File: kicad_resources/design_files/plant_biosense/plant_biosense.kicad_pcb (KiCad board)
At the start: 2 copper layers, 187 x 124.5 mm, 73 parts, among them J1 RJ45_Shielded, J2 RJ45_Shielded, U1 LM7805_TO220, U10 OP07, U11 TXS0108EPW, U12 OP07, U13 TL081, U14 NodeMCU1.0(ESP-12E), U15 ADS1115IDGS, U2 CD4051B, U3 CD4051B, U4 2S4P LI-ION BATTERY, U5 2S LI-ION BMS 10A, U7 XL4015, U8 AD620_instrumentation_amplifi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, U9 INA219AxD

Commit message: Initial public release: add CHL, docs, schematics
Adds CEREPHYTE Hardware License (CHL v1.0), NOTICE, CHANGELOG and THIRD_PARTY attribution; updates README. Adds multiple schematic PDFs under SCHEMATICS. Updates KiCad plant_biosense files (rev 4.2): date/revision bump, net/pad fixes (Net-(A1-D13)), pin type change, netclass/property and several wiring/no_connect adjustments. Prepares repository for public release and clarifies third-party licensing for included kicad-ESP8266 files.
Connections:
- A1 pad 28: unconnected-(A1-D13-Pad28) -> Net-(A1-D13)
- J2 pad 3: Net-(A1-D11) -> Net-(A1-D13)
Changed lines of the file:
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@@
 			(layers "*.Cu" "*.Mask")
 			(remove_unused_layers no)
-			(net "Net-(A1-D11)")
+			(net "Net-(A1-D13)")
 			(pintype "passive")
 		)
@@
 			(layers "*.Cu" "*.Mask")
 			(remove_unused_layers no)
-			(net "unconnected-(A1-D13-Pad28)")
+			(net "Net-(A1-D13)")
 			(pinfunction "D13_28")
-			(pintype "bidirectional+no_connect")
+			(pintype "bidirectional")
 		)
 		(pad "29" thru_hole oval

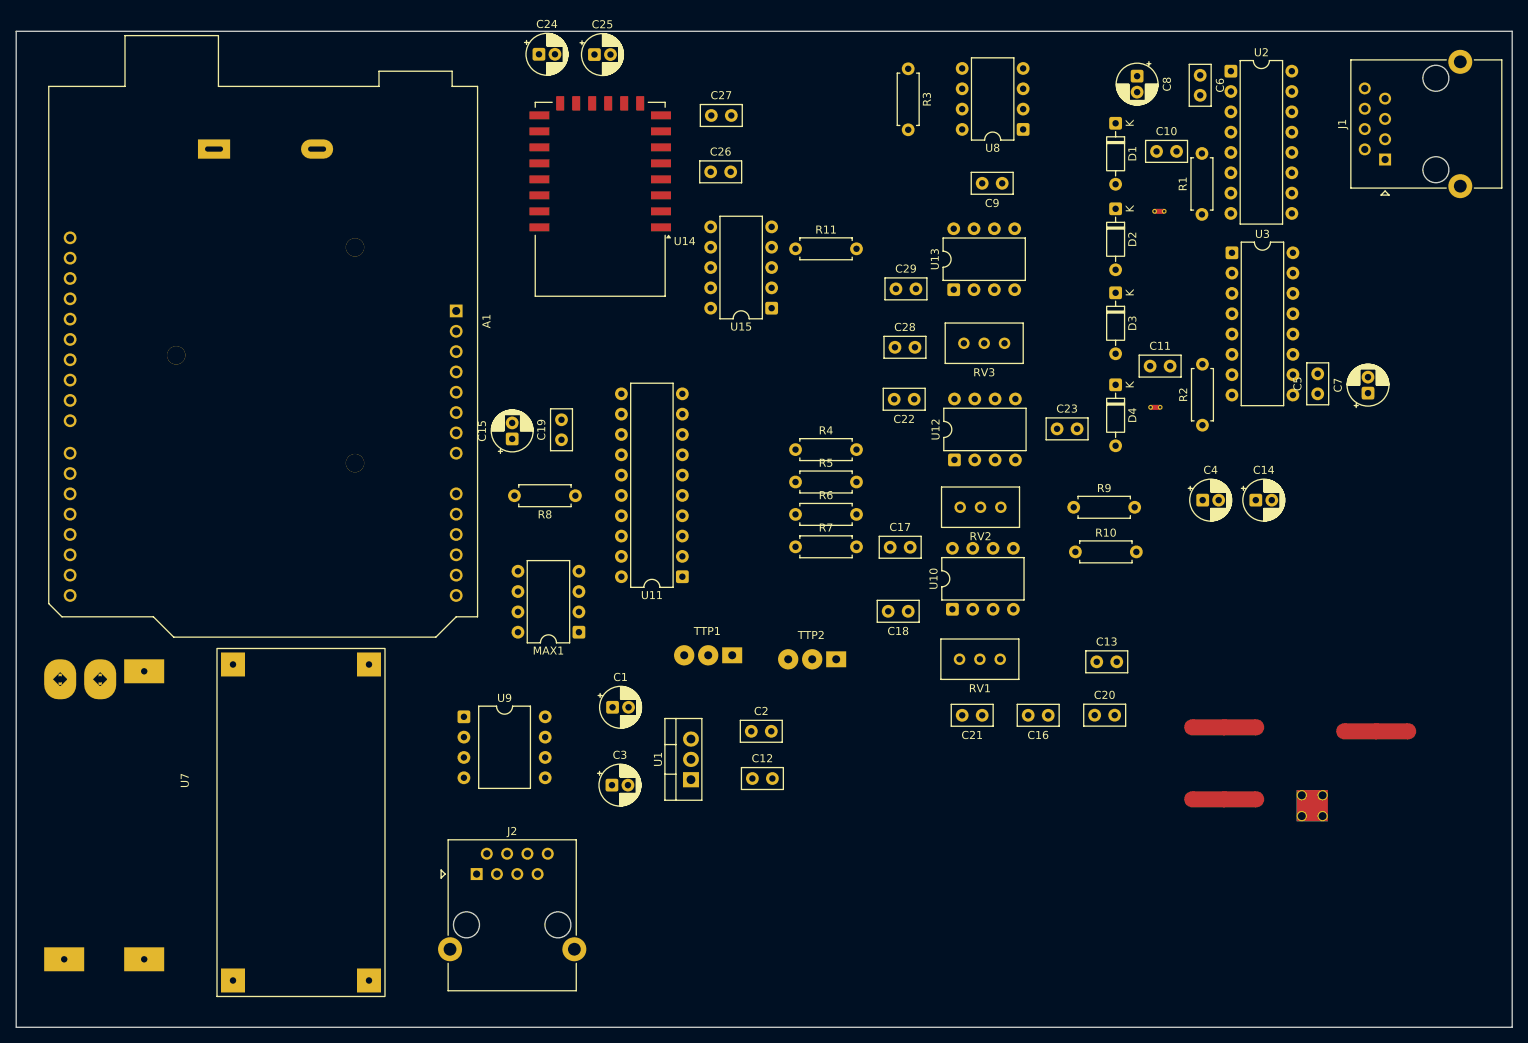
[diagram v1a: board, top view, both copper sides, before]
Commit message: 16 october 2026
Finalize CEREPHYTE Rev. 4.2 schematic architecture

- Finalize power supply, analog front-end, ADC, and microcontroller architecture
- Configure XL4015 buck converter for regulated 5V VDD
- Document INA219 and ADS1115 I2C addresses
- Define split analog/digital grounding topology
- Prepare schematic for physical protoboard implementation

Author: Omm Prakash Das
Date: 2026-10-16
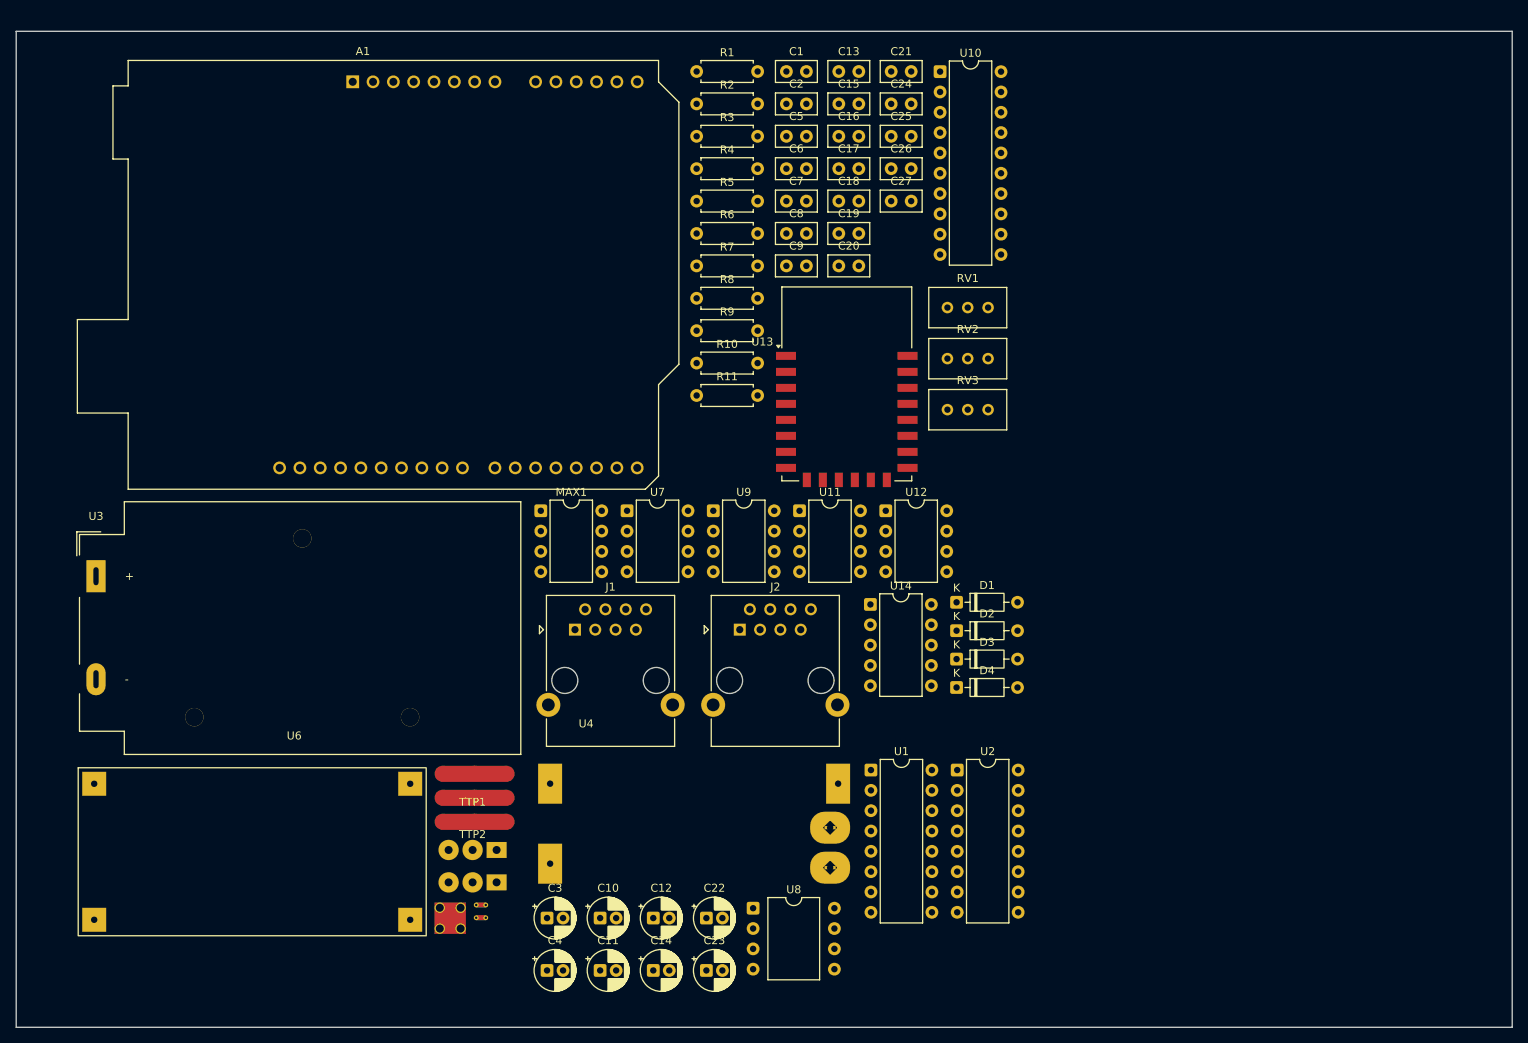
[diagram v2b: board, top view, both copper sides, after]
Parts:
- removed C28, C29: 0.1uf, Capacitor_THT:C_Disc_D5.0mm_W2.5mm_P2.50mm
- removed U15: ADS1115IDGS, Package_DIP:DIP-10_W7.62mm
- removed U5: 2S LI-ION BMS 10A, 2s LI-ION bms:2s LI-ION BMS 10A
- added U6: XL4015, XL4015 5A DC-DC Step Down Adjustable Power Supply Buck Module:XL4015 5A DC-DC Step Down Adjustable Power Supply Buck Mo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, F.Cu at (27.8, 111.6)
- C1, C15, C24, C25, C7, C8: value 10uf -> 0.1uf; footprint Capacitor_THT:CP_Radial_D5.0mm_P2.00mm -> Capacitor_THT:C_Disc_D5.0mm_W2.5mm_P2.50mm
- C10, C12, C22, C23: value 0.1uf -> 10uf; footprint Capacitor_THT:C_Disc_D5.0mm_W2.5mm_P2.50mm -> Capacitor_THT:CP_Radial_D5.0mm_P2.00mm
- C11: value 0.1uf -> 100uf; footprint Capacitor_THT:C_Disc_D5.0mm_W2.5mm_P2.50mm -> Capacitor_THT:CP_Radial_D5.0mm_P2.00mm
- C14: value 100uf -> 0.47uf
- C16, C20, C21: value 1uf -> 0.1uf
- C18, C19, C9: value 0.1uf -> 1uf
- C4: value 0.47uf -> 10uf
- U1: value LM7805_TO220 -> CD4051B; footprint Package_TO_SOT_THT:TO-220-3_Vertical -> Package_DIP:DIP-16_W7.62mm
- U10: value OP07 -> TXS0108EPW; footprint Package_DIP:DIP-8_W7.62mm -> Package_DIP:DIP-20_W7.62mm
- U11: value TXS0108EPW -> OP07; footprint Package_DIP:DIP-20_W7.62mm -> Package_DIP:DIP-8_W7.62mm
- U12: value OP07 -> TL081
- U13: value TL081 -> NodeMCU1.0(ESP-12E); footprint Package_DIP:DIP-8_W7.62mm -> RF_Module:ESP-12E
- U14: value NodeMCU1.0(ESP-12E) -> ADS1115IDGS; footprint RF_Module:ESP-12E -> Package_DIP:DIP-10_W7.62mm
- U3: value CD4051B -> 2S4P LI-ION BATTERY; footprint Package_DIP:DIP-16_W7.62mm -> Battery:BatteryHolder_MPD_BA9VPC_1xPP3
- U4: value 2S4P LI-ION BATTERY -> 2S LI-ION BMS 10A; footprint Battery:BatteryHolder_MPD_BA9VPC_1xPP3 -> 2s LI-ION bms:2s LI-ION BMS 10A; moved to F.Cu
- U7: value XL4015 -> AD620_instrumentation_amplifier_module; footprint XL4015 5A DC-DC Step Down Adjustable Power Supply Buck Module:XL4015 5A DC-DC Step Down Adjustable Power Supply Buck Mo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 -> Package_DIP:DIP-8_W7.62mm
- U8: value AD620_instrumentation_amplifier_module -> INA219AxD; footprint Package_DIP:DIP-8_W7.62mm -> Package_DIP:DIP-8_W10.16mm
- U9: value INA219AxD -> OP07; footprint Package_DIP:DIP-8_W10.16mm -> Package_DIP:DIP-8_W7.62mm
- moved U3 147.6 mm to (30.0, 87.6)
- moved NT1 121.3 mm to (77.5, 128.7)
- moved C10 118.4 mm to (93.0, 130.3)
- moved J1 117.1 mm to (89.8, 94.3), turned to 0 degrees
- moved NT4 113.0 mm to (77.3, 115.3)
- moved NT6 108.7 mm to (73.0, 129.1)
- moved NT2 105.7 mm to (77.5, 130.3)
- moved U8 103.0 mm to (112.1, 129.1), turned to 0 degrees
- moved C11 102.1 mm to (93.0, 136.9)
- moved C4 100.9 mm to (86.4, 136.9)
- moved C14 95.5 mm to (99.6, 136.9)
- moved NT3 93.9 mm to (77.3, 112.3)
- moved U2 93.8 mm to (137.6, 111.8)
- moved NT5 93.7 mm to (77.3, 118.3)
- moved U4 86.2 mm to (84.7, 110.5), turned to 0 degrees
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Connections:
- A1 pad 8: /PS_OUT+ -> /vdd
- C1 pad 2: GND -> GNDA
- C10 pad 1: /EESPC_out1 -> /vdd
- C10 pad 2: GNDA -> GND
- C11 pad 1: /EESPC_out2 -> GND
- C11 pad 2: GNDA -> /vee
- C12 pad 1: /PS_OUT+ -> /vdd
- C12 pad 2: /PS_OUT- -> GNDD
- C13 pad 1: Net-(U8-Vout) -> Net-(C13-Pad1)
- C13 pad 2: Net-(C13-Pad2) -> Net-(U9-+)
- C14 pad 1: GND -> /vdd
- C14 pad 2: /vee -> GND
- C15 pad 1: /PS_OUT+ -> GNDA
- C15 pad 2: GNDD -> Net-(U9-V+)
- C16 pad 1: Net-(C13-Pad2) -> /vee
- C16 pad 2: Net-(U10-+) -> GNDA
- C17 pad 1: GNDA -> /vdd
- C17 pad 2: Net-(U10-V+) -> GNDD
- C18 pad 1: /vee -> GNDA
- C18 pad 2: GNDA -> Net-(C18-Pad2)
- C19 pad 1: /PS_OUT+ -> GNDA
- C19 pad 2: GNDD -> Net-(U11-+)
- C2 pad 2: GND -> GNDA
- C20 pad 1: GNDA -> Net-(U11-V+)
- C20 pad 2: Net-(C20-Pad2) -> GNDA
- C21 pad 1: GNDA -> /vee
- C21 pad 2: Net-(U12-+) -> GNDA
- C22 pad 1: Net-(U12-V+) -> /vdd
- C22 pad 2: GNDA -> GNDD
- C23 pad 1: /vee -> /arduino5v
- C23 pad 2: GNDA -> GNDD
- C24 pad 1: /PS_OUT+ -> /arduino5v
- C25 pad 1: /arduino5v -> /vdd
- C26 pad 1: /arduino5v -> Net-(U12-V+)
- C26 pad 2: GNDD -> GNDA
- C27 pad 1: /PS_OUT+ -> /vee
- C27 pad 2: GNDD -> GNDA
- C3 pad 1: /PS_OUT+ -> /vdd
- C3 pad 2: GND -> GNDA
- C4 pad 1: /PS_OUT+ -> /vdd
- C4 pad 2: GND -> GNDA
- C5 pad 1: /vdd -> Net-(U7-vin)
- C6 pad 1: /vdd -> /EESPC_out1
- C7 pad 1: /vdd -> /EESPC_out2
- C8 pad 2: GNDA -> Net-(U6-OUT-)
- C9 pad 1: Net-(U8-vin) -> Net-(U7-Vout)
- C9 pad 2: GNDA -> Net-(C13-Pad1)
- NT3 pad 2: /PS_OUT- -> Net-(U6-OUT-)
- NT5 pad 1: Net-(U8-vin) -> Net-(U7-vin)
- NT5 pad 3: Net-(U10-V+) -> Net-(U9-V+)
- NT6 pad 1: Net-(U12-V+) -> Net-(U11-V+)
- NT6 pad 4: Net-(U13-V+) -> Net-(U12-V+)
- R10 pad 2: Net-(U12-+) -> Net-(U11-+)
- R11 pad 1: Net-(U15-AIN0) -> Net-(U14-AIN0)
- R3 pad 1: Net-(U8--v_out) -> Net-(U7--v_out)
- R4 pad 1: Net-(C13-Pad2) -> Net-(C13-Pad1)
- R5 pad 2: Net-(U10-+) -> Net-(U9-+)
- R6 pad 1: Net-(U10-+) -> Net-(U9-+)
- R7 pad 1: Net-(U10--) -> Net-(U9--)
- R7 pad 2: Net-(C20-Pad2) -> Net-(C18-Pad2)
- R9 pad 1: Net-(C20-Pad2) -> Net-(C18-Pad2)
- R9 pad 2: Net-(U12-+) -> Net-(U11-+)
- U1 pad 1: /PS_OUT+ -> /m4
- U1 pad 2: GND -> /m6
- U1 pad 3: /vdd -> /mux_out1
- U10 pad 1: Net-(RV1-Pad1) -> /LSDA
- U10 pad 2: Net-(U10--) -> /esp3.3v
- U10 pad 3: Net-(U10-+) -> /LSCL
- U10 pad 4: /vee -> /IOO1
- U10 pad 5: unconnected-(U10-NC-Pad5) -> /IOO2
- U10 pad 6: Net-(U10--) -> unconnected-(U10-A5-Pad6)
- U10 pad 7: Net-(U10-V+) -> unconnected-(U10-A6-Pad7)
- U10 pad 8: Net-(RV1-Pad3) -> /LSDA
- U11 pad 1: /LSDA -> Net-(RV2-Pad1)
- U11 pad 2: /esp3.3v -> Net-(U11--)
- U11 pad 3: /LSCL -> Net-(U11-+)
- U11 pad 4: /IOO1 -> /vee
- U11 pad 5: /IOO2 -> unconnected-(U11-NC-Pad5)
- U11 pad 6: unconnected-(U11-A5-Pad6) -> Net-(U11--)
- U11 pad 7: unconnected-(U11-A6-Pad7) -> Net-(U11-V+)
- U11 pad 8: /LSDA -> Net-(RV2-Pad3)
- U12 pad 1: Net-(RV2-Pad1) -> Net-(RV3-Pad1)
- U12 pad 2: Net-(U12--) -> /Aout
- U12 pad 3: Net-(U12-+) -> Net-(U11--)
- U12 pad 5: unconnected-(U12-NC-Pad5) -> Net-(RV3-Pad3)
- U12 pad 6: Net-(U12--) -> /Aout
- U12 pad 8: Net-(RV2-Pad3) -> unconnected-(U12-NC-Pad8)
- U13 pad 1: Net-(RV3-Pad1) -> unconnected-(U13-A0(ADC0)-Pad1)
- U13 pad 2: /Aout -> unconnected-(U13-RSV-Pad2)
- U13 pad 3: Net-(U12--) -> unconnected-(U13-RSV-Pad3)
- U13 pad 4: /vee -> unconnected-(U13-SD3(GPIO10)-Pad4)
- U13 pad 5: Net-(RV3-Pad3) -> unconnected-(U13-SD2(GPIO9)-Pad5)
- U13 pad 6: /Aout -> unconnected-(U13-SD1(MOSI)-Pad6)
- U13 pad 7: Net-(U13-V+) -> unconnected-(U13-CMD(CS)-Pad7)
- U14 pad 10: unconnected-(U14-GND-Pad10) -> /SCL
- U14 pad 3: unconnected-(U14-RSV-Pad3) -> GNDD
- U14 pad 4: unconnected-(U14-SD3(GPIO10)-Pad4) -> Net-(U14-AIN0)
- U14 pad 8: unconnected-(U14-SDO(MISO)-Pad8) -> /arduino5v
- U14 pad 9: unconnected-(U14-CLK(SCLK)-Pad9) -> /SDA
- U2 pad 10: /b1 -> /b2
- U2 pad 11: /a1 -> /a2
- U2 pad 3: /mux_out1 -> /mux_out2
- U2 pad 6: /INH1 -> /INH2
- U2 pad 9: /c1 -> /c2
- U3 pad 1: /m4 -> Net-(U3-CB+)
- U3 pad 2: /m6 -> Net-(U3-CB-)
- U4 pad 1: Net-(U4-CB+) -> /BP+
- U4 pad 2: Net-(U4-CB-) -> /BP-
- U7 pad 1: /BP+ -> Net-(U7-vin)
- U7 pad 2: /BP- -> GNDA
- U7 pad 3: /PS_OUT+ -> /EESPC_out2
- U7 pad 4: /PS_OUT- -> /EESPC_out1
- U8 pad 1: Net-(U8-vin) -> GNDD
- U8 pad 2: GNDA -> GNDD
- U8 pad 3: /EESPC_out2 -> /INASDA
- U8 pad 4: /EESPC_out1 -> /INASCL
- U8 pad 5: Net-(U8--v_out) -> /vdd
- U8 pad 6: GNDA -> GNDD
- U8 pad 7: Net-(U8-Vout) -> /BP+
- U8 pad 8: GNDA -> /BP+
- U9 pad 1: GNDD -> Net-(RV1-Pad1)
- U9 pad 2: GNDD -> Net-(U9--)
- U9 pad 3: /INASDA -> Net-(U9-+)
- U9 pad 4: /INASCL -> /vee
- U9 pad 5: /vdd -> unconnected-(U9-NC-Pad5)
- U9 pad 6: GNDD -> Net-(U9--)
- U9 pad 7: /BP+ -> Net-(U9-V+)
- U9 pad 8: /BP+ -> Net-(RV1-Pad3)
